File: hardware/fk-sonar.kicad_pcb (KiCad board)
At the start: 2 copper layers, 34.5 x 70.4 mm, 79 parts, among them J1 CONN_01x03, J10 CONN_01x02, J2 CONN_02x05_SWD, J3 RF-SMA-EDGE, J5 S2B-PH-SM4-TB, J6 CONN_01x04, J7 S2B-PH-SM4-TB, J8 CONN_01x03_SERIAL, J9 CONN_01x05, M1 MOUNT_HOLE, M3 MOUNT_HOLE, M4 MOUNT_HOLE, M6 MOUNT_HOLE, Q1 2N7002LT1G, SW1 SPNO, U1 ATSAMD21G18A-AU, U2 RFM95W, U3 BQ24074RGTT, U4 S25FL116K0XMFI041, U5 MAX1704XX, U6 MCP1700T-3302E/MB, U7 SK6812, U8 TPS2051B, Y1 FC-135

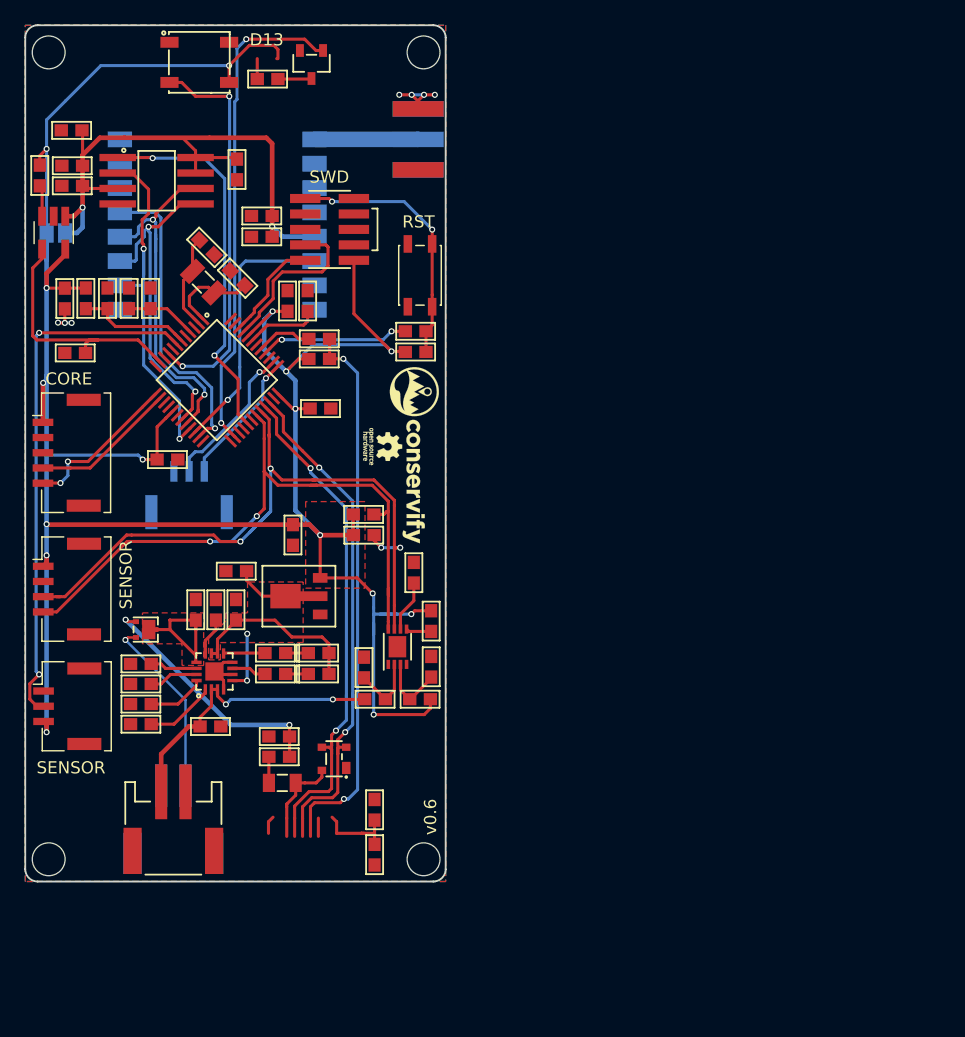
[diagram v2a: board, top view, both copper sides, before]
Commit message: Finished rough placement of components, starting trace routing
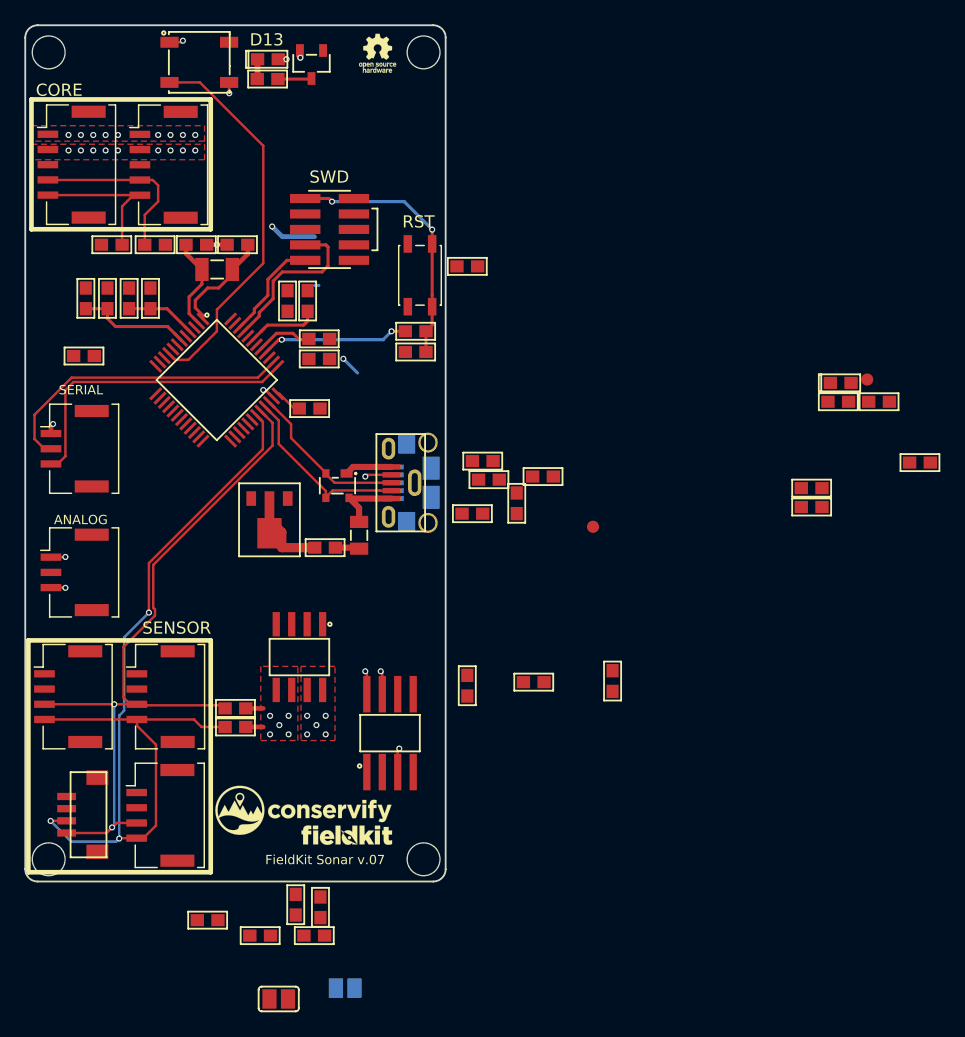
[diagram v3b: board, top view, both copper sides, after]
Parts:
- removed C21: 1uF, conservify:CAP-0603
- removed C22, C23: 100nF, conservify:CAP-0603
- removed C24: 10uF, conservify:CAP-0603
- removed D5: PMEG3020CPA, conservify:SOT-1016
- removed D6: PRTR5V0U2X, conservify:SOT-143B
- removed D7: Green, conservify:LED-0603
- removed D8: Red, conservify:LED-0603
- removed R18: 10K, conservify:RES-0603
- removed R19: 1K, conservify:RES-0603
- removed R20: 180R, conservify:RES-0603
- removed R21, R22: 4.7K, conservify:RES-0603
- removed U5: MAX1704XX, conservify:DFN-8-1EP_3x2mm_Pitch0.5mm
- removed U6: MCP1700T-3302E/MB, conservify:SOT-89
- removed U8: TPS2051B, conservify:SOT-23-5_HandSoldering
- added D1: Orange, conservify:LED-0603, F.Cu at (142.1, 65.0)
- added D2: PRTR5V0U2X, conservify:SOT-143B, F.Cu at (147.8, 100.1)
- added D3: Green, conservify:LED-0603, F.Cu at (189.2, 91.6)
- added G***: LOGO, conservify:LOGO_FK_NEGATIVE_2500, F.Cu at (148.6, 128.8)
- added J11: CONN_01x04, conservify:BM04B-SRSS-TB, F.Cu at (126.9, 127.1)
- added J12: CONN_01x04, conservify:Molex_CLIK-Mate_502382-0470_1x04_P1.25mm_Vertical, F.Cu at (125.7, 117.4)
- added J13: CONN_01x04, conservify:Molex_CLIK-Mate_502382-0470_1x04_P1.25mm_Vertical, F.Cu at (133.3, 117.4)
- added J4: MICRO-USB, conservify:USB_1051330011, F.Cu at (152.0, 99.8)
- added M2: FIDUCIAL, conservify:FIDUCIAL-1MM, F.Cu at (168.8, 103.4)
- added M5: FIDUCIAL, conservify:FIDUCIAL-1MM, F.Cu at (191.4, 91.3)
- C10: value 4.7uF -> 1uF
- C12: value 47uF -> 4.7uF
- C13: value 100nF -> 4.7nF
- C14: value 4.7nF -> 10uF
- C15, C16: value 4.7uF -> 100nF
- C17, C19: value 1uF -> 100nF
- C18: value 10nF -> 10uF
- J10: value CONN_01x02 -> CONN_01x05; footprint conservify:SJ_OPEN -> conservify:Molex_CLIK-Mate_502382-0570_1x05_P1.25mm_Vertical; moved to F.Cu
- J3: value RF-SMA-EDGE -> MICRO-USB; footprint conservify:RF-SMA-EDGE -> conservify:USB_10118193-0001LF-core-mod
- J5, J7: value S2B-PH-SM4-TB -> CONN_01x02; footprint conservify:S2B-PH-SM4-TB -> conservify:SJ_OPEN
- J8: moved to F.Cu
- R10: value 2K94 -> ?
- R11: value 2K2 -> 100K
- R12: value 330R -> 100K
- R13: value 1M -> 4.7K
- R16: value 10K -> 4.7K
- R17: value 2K2 -> 2k2
- R4: value 10K -> 1M
- R5: value 10K -> 330R
- R6: value 10K -> 100K
- R7: value 1K18 -> 10K
- R8: value 46K4 -> ?
- R9: value 100K -> 10K
- U2: value RFM95W -> MCP1700T-3302E/MB; footprint conservify:RFM9xW -> conservify:SOT-89; moved to F.Cu
- U3: value BQ24074RGTT -> TPS2052B; footprint conservify:QFN-16_3x3mm -> conservify:SOIC-8-N
- moved R7 59.1 mm to (195.7, 98.2), turned to 0 degrees
- moved C15 58.1 mm to (189.0, 93.2)
- moved C10 56.4 mm to (192.3, 93.2), turned to 0 degrees
- moved R13 54.6 mm to (129.3, 80.3), turned to 180 degrees
- moved C20 52.1 mm to (170.4, 116.1)
- moved U4 49.3 mm to (152.1, 120.4), turned to 90 degrees
- moved C16 48.3 mm to (186.8, 100.3), turned to 0 degrees
- moved R6 48.1 mm to (164.7, 99.3)
- moved R4 47.6 mm to (162.6, 101.5)
- moved R17 45.7 mm to (186.8, 101.8)
- moved R5 35.2 mm to (158.9, 102.4)
- moved G*** 32.3 mm to (151.1, 64.5), turned to 0 degrees
- moved C19 31.4 mm to (158.5, 82.0)
- moved G*** 30.6 mm to (145.0, 126.7), turned to 0 degrees
- moved C11 28.4 mm to (164.0, 116.2), turned to 0 degrees
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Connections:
- C11 pad 1: GND -> 3V3
- C11 pad 2: VEXT -> GND
- C12 pad 1: /PERIPH_3V3 -> 5V0
- C13 pad 1: /PERIPH_3V3 -> Net-(C13-Pad1)
- C14 pad 1: Net-(C14-Pad1) -> /PERIPH_3V3
- C15 pad 1: VBAT -> 3V3
- C16 pad 1: VBUS -> /PERIPH_3V3
- C17 pad 1: Net-(C17-Pad1) -> /SENSOR_3V3
- C18 pad 1: GND -> /SENSOR_3V3
- C18 pad 2: Net-(C18-Pad2) -> GND
- C19 pad 1: VBUS -> /RST
- J10 pad 2: /PERIPH_3V3 -> GND
- J3 pad 1: Net-(J3-Pad1) -> VUSB
- J3 pad 2: GND -> /USB-
- J3 pad 3: GND -> /USB+
- J3 pad 4: GND -> Net-(J3-Pad4)
- J5 pad 1: VBAT -> 3V3
- J5 pad 2: GND -> /PERIPH_3V3
- J6 pad 1: 3V3 -> /SENSOR_3V3
- J7 pad 1: VIN -> 3V3
- J7 pad 2: GND -> /SENSOR_3V3
- R10 pad 1: GND -> /D7_SENSOR_EN
- R10 pad 2: Net-(R10-Pad2) -> GND
- R11 pad 1: GND -> /PERIPH_3V3
- R11 pad 2: Net-(R11-Pad2) -> GND
- R12 pad 1: Net-(J4-Pad4) -> /SENSOR_3V3
- R12 pad 2: /USB_ID -> GND
- R13 pad 1: Net-(C14-Pad1) -> /SDA3
- R13 pad 2: GND -> 3V3
- R14 pad 1: 3V3 -> /SCL3
- R14 pad 2: /SDA1 -> 3V3
- R15 pad 1: 3V3 -> /SDA1
- R15 pad 2: /SCL1 -> /SENSOR_3V3
- R16 pad 1: /PG -> /SCL1
- R16 pad 2: Net-(D7-Pad1) -> /SENSOR_3V3
- R17 pad 1: /CHG -> Net-(D3-Pad1)
- R17 pad 2: Net-(D8-Pad1) -> GND
- R4 pad 1: Net-(R4-Pad1) -> Net-(C13-Pad1)
- R4 pad 2: 3V3 -> GND
- R5 pad 1: GND -> Net-(J3-Pad4)
- R5 pad 2: /D8_PERIPH_EN -> /USB_ID
- R6 pad 1: GND -> 3V3
- R6 pad 2: /PERIPH_3V3 -> Net-(J3-Pad4)
- R7 pad 1: GND -> Net-(R7-Pad1)
- R7 pad 2: Net-(R7-Pad2) -> 3V3
- R8 pad 1: GND -> /D8_PERIPH_EN
- R8 pad 2: Net-(R8-Pad2) -> GND
- R9 pad 1: Net-(J4-Pad4) -> Net-(R9-Pad1)
- U2 pad 2: /MISO -> 5V0
- U2 pad 3: /MOSI -> 3V3
- U3 pad 1: Net-(R18-Pad1) -> GND
- U3 pad 2: VBAT -> 3V3
- U3 pad 3: VBAT -> /D8_PERIPH_EN
- U3 pad 4: GND -> /D7_SENSOR_EN
- U3 pad 5: VBUS -> Net-(R9-Pad1)
- U3 pad 6: GND -> /SENSOR_3V3
- U3 pad 7: /PG -> /PERIPH_3V3
- U3 pad 8: GND -> Net-(R7-Pad1)
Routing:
- net 3V3: track 214.4 -> 5.02 mm, vias 16 -> 12
- net /PERIPH_3V3: track 55.0 -> 9.68 mm, vias 2 -> 9
- net Net-(J4-Pad4): track 45.6 -> 1.66 mm, vias 2 -> 1
- net /A1: track 43.8 -> 0.00 mm, vias 2 -> 0
- net /D13: track 40.7 -> 0.00 mm, vias 2 -> 0
- net /MISO: track 31.5 -> 0.00 mm, vias 2 -> 0
- net /D6_FLASH_CS: track 31.3 -> 0.00 mm, vias 2 -> 0
- net /SCK: track 30.2 -> 0.00 mm, vias 2 -> 0
- net /USB+: track 43.2 -> 13.5 mm, vias 2 -> 0
- net /MOSI: track 27.9 -> 0.00 mm, vias 2 -> 0
- net /USB-: track 42.5 -> 15.2 mm, vias 2 -> 0
- net VBUS: track 26.5 -> 0.00 mm, vias 2 -> 0
- net VBAT: track 25.8 -> 0.00 mm, vias 2 -> 0
- net /D2_RADIO_CS: track 25.2 -> 0.00 mm, vias 1 -> 0
- net /SDA1: track 53.6 -> 75.6 mm, vias 2 -> 3
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- added copper zone on F.Cu, net /PERIPH_3V3
- added copper zone on PWR, net /PERIPH_3V3
- added copper zone on F.Cu, net /SENSOR_3V3
- added copper zone on PWR, net /SENSOR_3V3
- added copper zone on PWR, net 3V3
- added copper zone on GND, net GND
- removed copper zone on B.Cu, net GND
- removed copper zone on F.Cu, net VBUS
- removed copper zone on F.Cu, net VEXT
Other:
- copper layers 2 -> 4
- board text added: "ANALOG"
- board text added: "FieldKit Sonar v.07"
- board text added: "SERIAL"
- board text removed: "v0.6"

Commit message: Finished routing traces, starting DRC
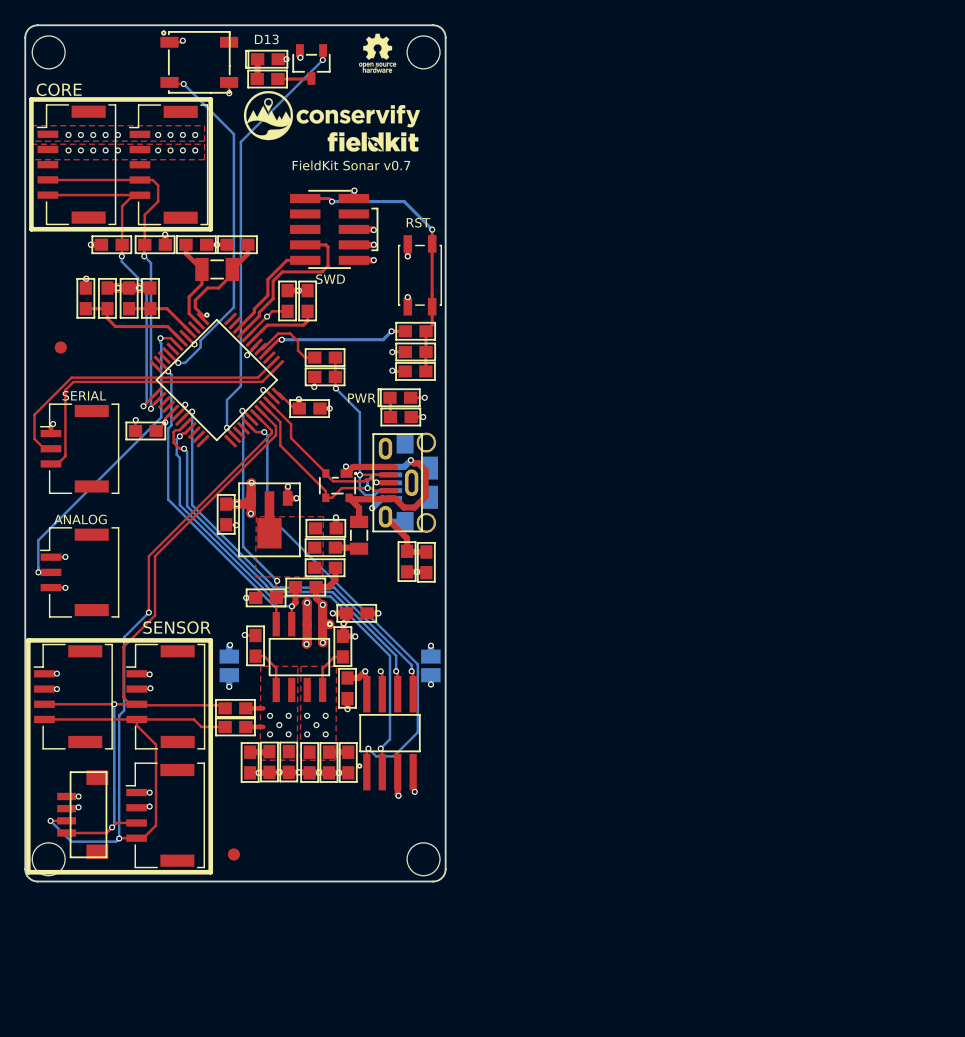
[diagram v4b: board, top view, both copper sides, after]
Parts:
- J5: moved to B.Cu
- moved M5 66.3 mm to (125.1, 88.7)
- moved G*** 57.1 mm to (147.4, 69.7)
- moved G*** 57.0 mm to (150.7, 71.8)
- moved R7 49.8 mm to (148.3, 113.3), turned to 90 degrees
- moved C10 46.6 mm to (146.9, 103.6)
- moved C16 45.6 mm to (147.1, 122.8), turned to 270 degrees
- moved C15 43.2 mm to (149.4, 110.6)
- moved M2 39.9 mm to (139.3, 130.4)
- moved D3 36.2 mm to (153.0, 92.8)
- moved R12 35.3 mm to (140.7, 122.8), turned to 270 degrees
- moved R17 34.6 mm to (153.0, 94.4)
- moved J5 30.1 mm to (155.5, 114.9), turned to 270 degrees
- moved C11 28.8 mm to (138.7, 102.4), turned to 270 degrees
- moved R8 28.6 mm to (145.2, 108.4)
- moved J7 28.1 mm to (138.9, 114.9), turned to 270 degrees
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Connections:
- J12 pad 2: Net-(J12-Pad2) -> GND
- J13 pad 2: Net-(J13-Pad2) -> GND
- U1 pad 30: /D7 -> /D7_SENSOR_EN
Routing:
- net GND: track 10.5 -> 61.2 mm, vias 15 -> 53
- net /MISO: track 0.00 -> 38.8 mm, vias 0 -> 2
- net /D6_FLASH_CS: track 0.00 -> 38.7 mm, vias 0 -> 2
- net /D13: track 0.00 -> 35.3 mm, vias 0 -> 2
- net /MOSI: track 0.00 -> 34.8 mm, vias 0 -> 2
- net /SCK: track 0.00 -> 33.5 mm, vias 0 -> 2
- net 3V3: track 5.02 -> 34.5 mm, vias 12 -> 33
- net /D8_PERIPH_EN: track 0.00 -> 28.8 mm, vias 0 -> 2
- net /A1: track 0.00 -> 26.1 mm, vias 0 -> 2
- net /D7_SENSOR_EN: track 0.00 -> 19.8 mm, vias 0 -> 2
- net /SDA3: track 12.6 -> 28.2 mm, vias 0 -> 2
- net Net-(J3-Pad4): track 2.22 -> 17.2 mm, vias 1 -> 2
- net /SCL3: track 15.1 -> 30.0 mm, vias 0 -> 2
- net VUSB: track 5.85 -> 14.9 mm, vias 0 -> 1
- net Net-(C13-Pad1): track 0.00 -> 6.95 mm
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- added copper zone on F.Cu, net 5V0
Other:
- rule pad_to_mask_clearance: 0.1016 -> 0
- board text added: "FieldKit Sonar v0.7"
- board text added: "PWR"
- board text removed: "DEBUG"
- board text removed: "FieldKit Sonar v.07"

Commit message: Finished DRC
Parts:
- moved G*** 1.29 mm to (151.2, 73.0)
- moved G*** 1.19 mm to (147.9, 70.7)
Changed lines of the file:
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@@
   )
   (module conservify:conservify_text_negative_5000 locked (layer F.Cu)
-    (at 147.3835 69.6595)
+    (at 147.8915 70.739)
     (fp_text reference G*** (at 0 0) (layer F.SilkS) hide
       (effects (font (size 1.524 1.524) (thickness 0.3)))
@@
   )
   (module conservify:LOGO_FK_NEGATIVE_2500 locked (layer F.Cu)
-    (at 150.749 71.8185)
+    (at 151.1935 73.025)
     (fp_text reference G*** (at 0 0) (layer F.SilkS) hide
       (effects (font (size 1.524 1.524) (thickness 0.3)))
@@
     (effects (font (size 0.762 0.762) (thickness 0.1524)))
   )
-  (gr_text "FieldKit Sonar v0.7" (at 148.971 73.787) (layer F.SilkS)
+  (gr_text "FieldKit Sonar v0.7" (at 147.32 131.3815) (layer F.SilkS)
     (effects (font (size 0.762 0.762) (thickness 0.1524)))
   )
@@
     (effects (font (size 0.762 0.762) (thickness 0.1524)))
   )
-  (gr_text CORE (at 124.968 67.564) (layer F.SilkS)
+  (gr_text CORE (at 124.841 79.883) (layer F.SilkS)
     (effects (font (size 1 1) (thickness 0.2)))
   )
@@
     (polygon
       (pts
-        (xy 122.174 61.976) (xy 156.718 61.976) (xy 156.718 114.808) (xy 122.428 114.808)
+        (xy 122.174 61.976) (xy 156.718 61.976) (xy 156.718 114.554) (xy 122.174 114.554)
       )
     )
@@
     (polygon
       (pts
-        (xy 144.653 114.935) (xy 144.526 132.334) (xy 122.174 132.588) (xy 122.301 114.935)
+        (xy 144.526 114.935) (xy 144.526 132.588) (xy 122.047 132.588) (xy 122.174 114.935)
       )
     )
@@
     (polygon
       (pts
-        (xy 144.8308 114.9096) (xy 144.78 122.6185) (xy 147.701 122.6185) (xy 147.7518 114.9096)
+        (xy 144.78 114.808) (xy 144.78 122.682) (xy 147.828 122.682) (xy 147.828 114.808)
       )
     )
@@
     (polygon
       (pts
-        (xy 144.78 114.935) (xy 144.78 132.588) (xy 156.718 132.588) (xy 156.718 114.935)
+        (xy 144.78 114.808) (xy 144.78 132.588) (xy 156.718 132.588) (xy 156.718 114.808)
       )
     )
@@
     (polygon
       (pts
-        (xy 141.5288 114.9096) (xy 141.478 122.6185) (xy 144.526 122.6185) (xy 144.5768 114.9096)
+        (xy 141.478 114.808) (xy 141.478 122.6185) (xy 144.526 122.6185) (xy 144.526 114.808)
       )
     )
